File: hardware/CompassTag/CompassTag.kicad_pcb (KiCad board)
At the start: 2 copper layers, 16 x 9 mm, 22 parts, among them J201 CONN_02X04, J301 Conn_01x01, J302 Conn_01x01, J303 Conn_01x01, J304 Conn_01x01, J401 CONN_01X02, Q501 Q_NPN_BEC, U1 at25ex321D-UUN, U3 LIS2DU12TR, U302 stm32l431kc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

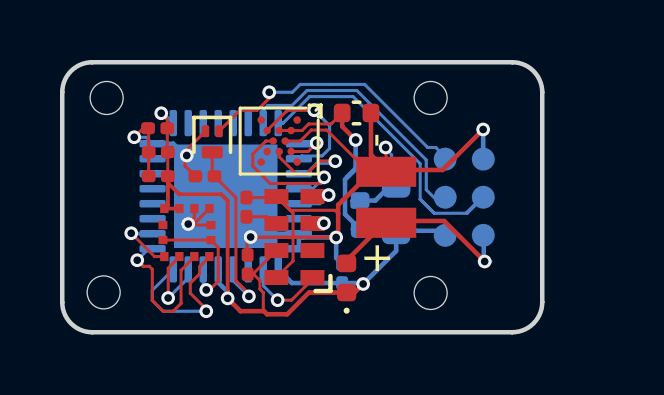
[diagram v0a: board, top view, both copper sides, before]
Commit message: designed compass tag
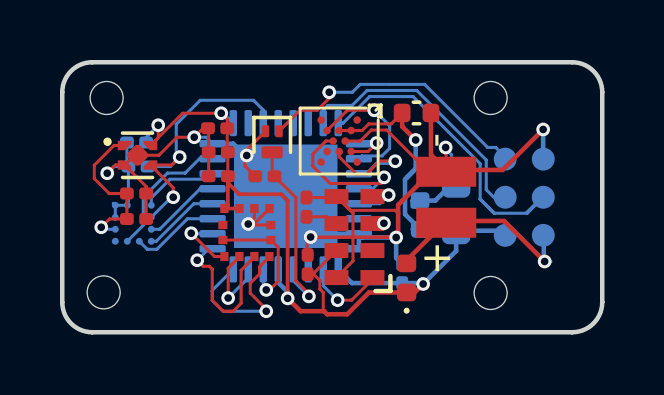
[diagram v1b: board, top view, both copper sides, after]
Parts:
- added C5: 0.1uf, Capacitor_SMD:C_0201_0603Metric, B.Cu at (142.5, 107.5)
- added C7: 1uf, Capacitor_SMD:C_0201_0603Metric, B.Cu at (142.5, 106.7)
- added C8: 1uf, Capacitor_SMD:C_0201_0603Metric, F.Cu at (142.5, 109.2)
- added C9: 0.1uf, Capacitor_SMD:C_0201_0603Metric, F.Cu at (142.5, 108.4)
- added U2: AK09940A, AccelTag:AK09940a, B.Cu at (142.4, 109.4)
- added U4: TPS7A2018PDQN, Package_SON:Texas_X2SON-4_1x1mm_P0.65mm, F.Cu at (142.5, 107.1)
- moved C1 2.00 mm to (145.2, 107.8)
- moved C2 2.00 mm to (145.2, 106.2)
- moved C3 2.00 mm to (145.2, 107.0)
- moved C4 2.00 mm to (151.8, 105.7)
- moved C404 2.00 mm to (151.9, 109.1)
- moved C501 2.00 mm to (151.3, 111.0)
- moved C502 2.00 mm to (146.8, 107.8)
- moved C503 2.00 mm to (148.2, 110.7)
- moved C6 2.00 mm to (153.1, 108.8)
- moved D401 2.00 mm to (151.5, 111.2)
- moved J201 2.00 mm to (155.4, 108.5)
- moved J301 2.00 mm to (154.3, 111.7)
- moved J302 2.00 mm to (154.3, 105.2)
- moved J401 2.00 mm to (152.8, 108.5)
- moved Q501 2.00 mm to (147.0, 106.7)
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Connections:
- U302 pad 11: unconnected-(U302-PA5-Pad11) -> /AK_CK
- U302 pad 12: unconnected-(U302-PA6-Pad12) -> /AK_MISO
- U302 pad 13: unconnected-(U302-PA7-Pad13) -> /AK_MOSI
- U302 pad 14: unconnected-(U302-PB0-Pad14) -> /AK_RSTN
- U302 pad 15: unconnected-(U302-PB1-Pad15) -> /AK_CS
- U302 pad 19: unconnected-(U302-PA9-Pad19) -> /AK_PWR
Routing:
- net /AK_PWR: track 0.00 -> 9.63 mm, vias 0 -> 2
- net GND: track 51.0 -> 60.4 mm, vias 7 -> 8
- net +1V8: track 0.00 -> 5.37 mm, vias 0 -> 1
- net /AK_CS: track 0.00 -> 4.53 mm
- net VIN: track 35.1 -> 39.4 mm, vias 4 -> 5
- net /AK_CK: track 0.00 -> 3.05 mm
- net /AK_MISO: track 0.00 -> 2.64 mm
- net /AK_RSTN: track 0.00 -> 2.62 mm
- net /AK_MOSI: track 0.00 -> 2.60 mm
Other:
- board size 16 x 9 mm -> 18 x 9 mm
